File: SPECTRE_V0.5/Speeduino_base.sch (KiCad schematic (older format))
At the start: 209 parts, among them J1 Conn_01x04_Male, J2 Conn_02x04_Odd_Even, J3 Conn_01x06_Male, Q1 2N7002, Q10 BSP78, Q11 BSP78, Q12 BSP78, Q13 BSP78, Q14 BSP78, Q15 BSP78, Q16 SMD-MOSFET-N-CH-55V-2.1A-AO34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, Q17 AO3401A, Q18 BSP78, Q19 SMD-MOSFET-N-CH-55V-2.1A-AO34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, Q2 CJ2302, Q20 AO3401A, Q21 SMD-MOSFET-N-CH-55V-2.1A-AO34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, Q22 SMD-MOSFET-N-CH-55V-2.1A-AO34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, Q23 AO3401A, Q24 AO3401A, Q25 BSP78, Q26 BSP78, Q3 CJ2302, Q4 CJ2302, Q5 BSP78, Q6 BSP78, Q7 CJ2302, Q8 CJ2302, Q9 CJ2302, U1 MAX9926UAEE+, U2 molex_48pin, U3 LM78M05_TO220, U4 MAX3232

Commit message: Somem ore routing V0.5
Routing board V0.5
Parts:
- added JP5: Jumper_NC_Small, Jumper:SolderJumper-2_P1.3mm_Bridged_Pad1.0x1.5mm, symbol Device:Jumper_NC_Small
- added R97: 120, Speeduino_base:R0603, symbol Speeduino_base-eagle-import:SMD-RES-470R-5%-1_10W(0603)
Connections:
- wire segments 549 -> 559
- no-connect marks 54 -> 51
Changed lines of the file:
@@
 Wire Wire Line
 	9900 11100 10350 11100
-Text GLabel 11300 11100 2    50   Input ~ 0
+Text GLabel 10350 11100 2    50   Input ~ 0
 VBAT_F1
 Text GLabel 10450 10700 2    50   Input ~ 0
@@
 NoConn ~ 9600 2800
 NoConn ~ 10500 4000
-NoConn ~ 10200 4800
 NoConn ~ 10200 4900
 NoConn ~ 10200 5000
 NoConn ~ 12050 5000
 NoConn ~ 10500 5000
-NoConn ~ 10500 4500
-NoConn ~ 10200 4500
-NoConn ~ 10500 4400
 NoConn ~ 12050 3300
 NoConn ~ 11750 3400
@@
 $EndComp
 NoConn ~ 11000 6450
-Text GLabel 12050 6250 2    50   Output ~ 0
+Text GLabel 12350 6100 2    50   BiDi ~ 0
 CANL
-Text GLabel 12050 6350 2    50   Output ~ 0
+Text GLabel 12350 6500 2    50   BiDi ~ 0
 CANH
-Text GLabel 6900 1400 3    50   Input ~ 0
+Text GLabel 6900 1400 3    50   BiDi ~ 0
 CANH
-Text GLabel 8700 1400 3    50   Input ~ 0
+Text GLabel 8700 1400 3    50   BiDi ~ 0
 CANL
 Text GLabel 11500 5900 2    50   Input ~ 0
@@
 Wire Wire Line
 	5550 1750 5550 1400
+$Comp
+L Device:Jumper_NC_Small JP5
+U 1 1 5E9CEF08
+P 12450 6400
+F 0 "JP5" H 12450 6612 50  0000 C CNN
+F 1 "Jumper_NC_Small" H 12450 6521 50  0000 C CNN
+F 2 "Jumper:SolderJumper-2_P1.3mm_Bridged_Pad1.0x1.5mm" H 12450 6400 50  0001 C CNN
+F 3 "~" H 12450 6400 50  0001 C CNN
+	1    12450 6400
+	1    0    0    -1
+$EndComp
+$Comp
+L Speeduino_base-eagle-import:SMD-RES-470R-5%-1_10W(0603) R97
+U 1 1 5E9D0C9F
+P 12450 6250
+F 0 "R97" H 12300 6300 42  0000 L BNN
+F 1 "120" H 12300 6150 42  0000 L BNN
+F 2 "Speeduino_base:R0603" H 12450 6250 50  0001 C CNN
+F 3 "" H 12450 6250 50  0001 C CNN
+	1    12450 6250
+	-1   0    0    1
+$EndComp
+Wire Wire Line
+	12600 6250 12650 6250
+Wire Wire Line
+	12650 6250 12650 6400
+Wire Wire Line
+	12650 6400 12550 6400
+Wire Wire Line
+	12350 6100 12300 6100
+Wire Wire Line
+	12300 6100 12300 6250
+Wire Wire Line
+	12350 6400 12350 6500
+Wire Wire Line
+	12050 6350 12250 6350
+Wire Wire Line
+	12250 6350 12250 6400
+Wire Wire Line
+	12250 6400 12350 6400
+Connection ~ 12350 6400
+Wire Wire Line
+	12300 6250 12050 6250
+Connection ~ 12300 6250
+NoConn ~ 10200 4500
 $EndSCHEMATC

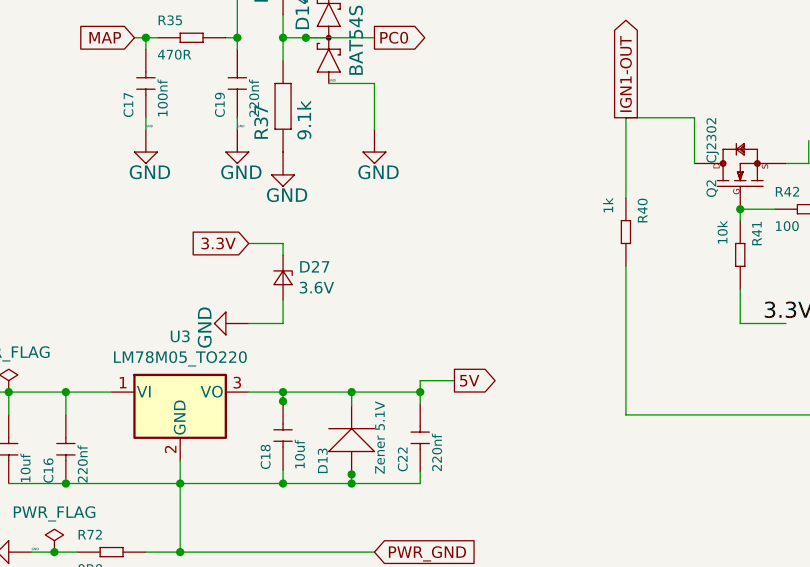
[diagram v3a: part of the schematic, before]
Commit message: 3.3V power protection
Extra protection for the 3.3volt supply. TL431 is used for this.
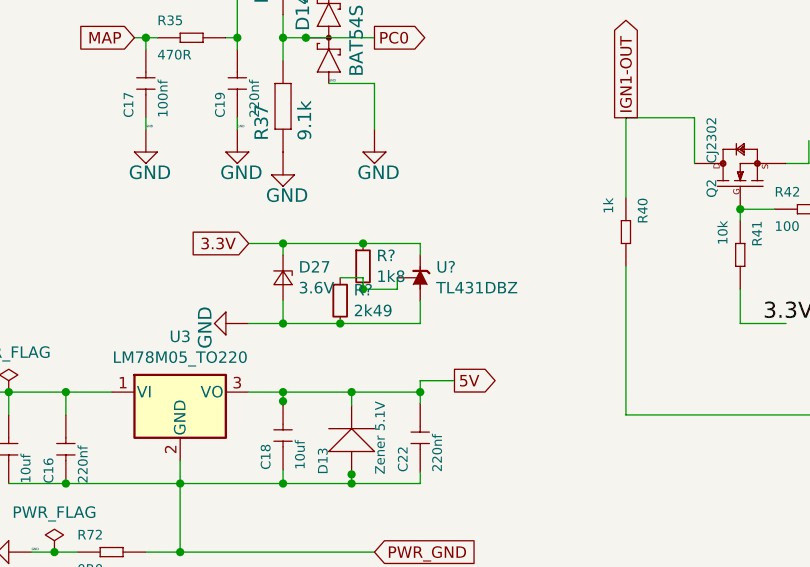
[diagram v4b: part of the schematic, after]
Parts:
- added R?: 1k8, Resistor_SMD:R_0603_1608Metric_Pad1.05x0.95mm_HandSolder, symbol Device:R_Small
- added R?: 2k49, Resistor_SMD:R_0603_1608Metric_Pad1.05x0.95mm_HandSolder, symbol Device:R_Small
- added U?: TL431DBZ, Package_TO_SOT_SMD:SOT-23, symbol Reference_Voltage:TL431DBZ
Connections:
- wire segments 559 -> 569
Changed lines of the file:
@@
 Connection ~ 12300 6250
 NoConn ~ 10200 4500
+$Comp
+L Reference_Voltage:TL431DBZ U?
+U 1 1 5EC38137
+P 3750 10300
+F 0 "U?" V 3796 10230 50  0000 R CNN
+F 1 "TL431DBZ" V 3705 10230 50  0000 R CNN
+F 2 "Package_TO_SOT_SMD:SOT-23" H 3750 10150 50  0001 C CIN
+F 3 "http://www.ti.com/lit/ds/symlink/tl431.pdf" H 3750 10300 50  0001 C CIN
+	1    3750 10300
+	0    -1   -1   0
+$EndComp
+Wire Wire Line
+	3150 10150 3500 10150
+Wire Wire Line
+	3750 10150 3750 10200
+Connection ~ 3150 10150
+Wire Wire Line
+	3750 10400 3750 10500
+Wire Wire Line
+	3750 10500 3400 10500
+Connection ~ 3150 10500
+$Comp
+L Device:R_Small R?
+U 1 1 5ECE80FF
+P 3500 10250
+F 0 "R?" H 3559 10296 50  0000 L CNN
+F 1 "1k8" H 3559 10205 50  0000 L CNN
+F 2 "Resistor_SMD:R_0603_1608Metric_Pad1.05x0.95mm_HandSolder" H 3500 10250 50  0001 C CNN
+F 3 "~" H 3500 10250 50  0001 C CNN
+	1    3500 10250
+	1    0    0    -1
+$EndComp
+Connection ~ 3500 10150
+Wire Wire Line
+	3500 10150 3750 10150
+$Comp
+L Device:R_Small R?
+U 1 1 5ECEB0D8
+P 3400 10400
+F 0 "R?" H 3459 10446 50  0000 L CNN
+F 1 "2k49" H 3459 10355 50  0000 L CNN
+F 2 "Resistor_SMD:R_0603_1608Metric_Pad1.05x0.95mm_HandSolder" H 3400 10400 50  0001 C CNN
+F 3 "~" H 3400 10400 50  0001 C CNN
+	1    3400 10400
+	1    0    0    -1
+$EndComp
+Connection ~ 3400 10500
+Wire Wire Line
+	3400 10500 3150 10500
+Wire Wire Line
+	3400 10300 3500 10300
+Wire Wire Line
+	3500 10300 3500 10350
+Wire Wire Line
+	3500 10350 3650 10350
+Wire Wire Line
+	3650 10350 3650 10300
+Connection ~ 3500 10350
 $EndSCHEMATC

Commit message: Update Speeduino_base.sch
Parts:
- gave numbers to parts that had none: 3
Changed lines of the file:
@@
 NoConn ~ 10200 4500
 $Comp
-L Reference_Voltage:TL431DBZ U?
+L Reference_Voltage:TL431DBZ U5
 U 1 1 5EC38137
 P 3750 10300
-F 0 "U?" V 3796 10230 50  0000 R CNN
+F 0 "U5" V 3796 10230 50  0000 R CNN
 F 1 "TL431DBZ" V 3705 10230 50  0000 R CNN
 F 2 "Package_TO_SOT_SMD:SOT-23" H 3750 10150 50  0001 C CIN
@@
 Connection ~ 3150 10500
 $Comp
-L Device:R_Small R?
+L Device:R_Small R99
 U 1 1 5ECE80FF
 P 3500 10250
-F 0 "R?" H 3559 10296 50  0000 L CNN
+F 0 "R99" H 3559 10296 50  0000 L CNN
 F 1 "1k8" H 3559 10205 50  0000 L CNN
 F 2 "Resistor_SMD:R_0603_1608Metric_Pad1.05x0.95mm_HandSolder" H 3500 10250 50  0001 C CNN
@@
 	3500 10150 3750 10150
 $Comp
-L Device:R_Small R?
+L Device:R_Small R98
 U 1 1 5ECEB0D8
 P 3400 10400
-F 0 "R?" H 3459 10446 50  0000 L CNN
+F 0 "R98" H 3459 10446 50  0000 L CNN
 F 1 "2k49" H 3459 10355 50  0000 L CNN
 F 2 "Resistor_SMD:R_0603_1608Metric_Pad1.05x0.95mm_HandSolder" H 3400 10400 50  0001 C CNN

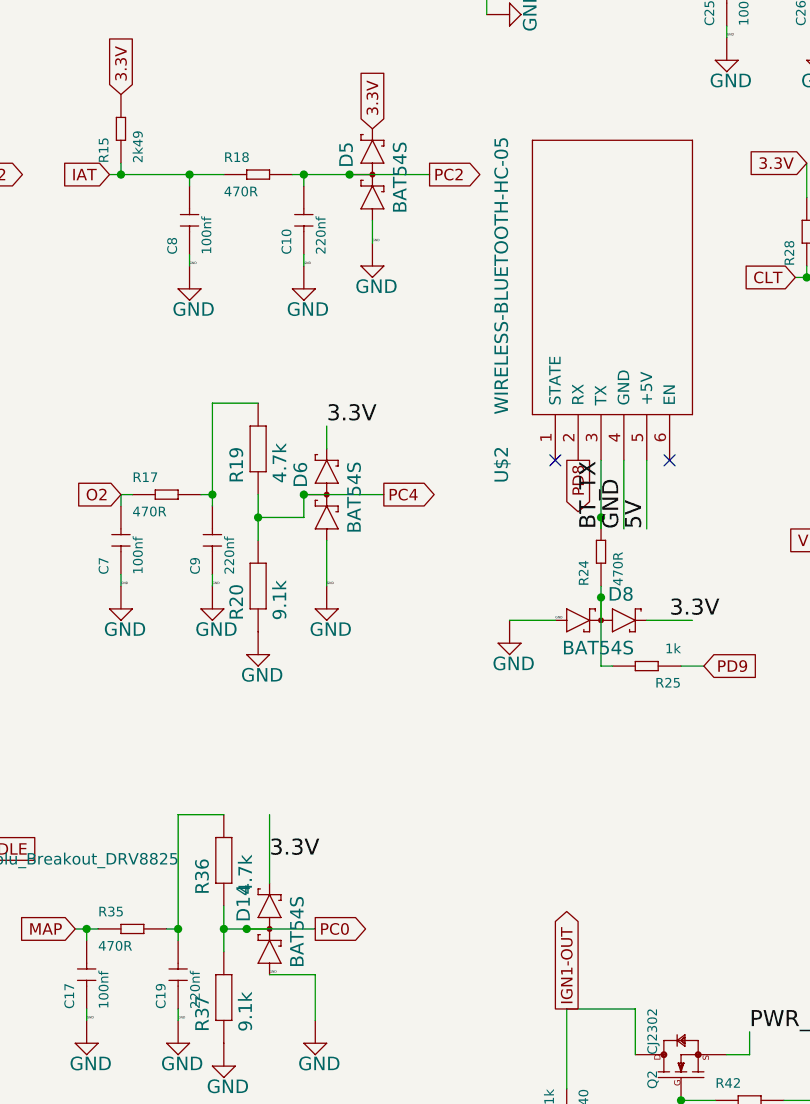
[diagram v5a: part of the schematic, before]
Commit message: V0.5 fully routed
Routed the whole SPECTRE V0.5 board
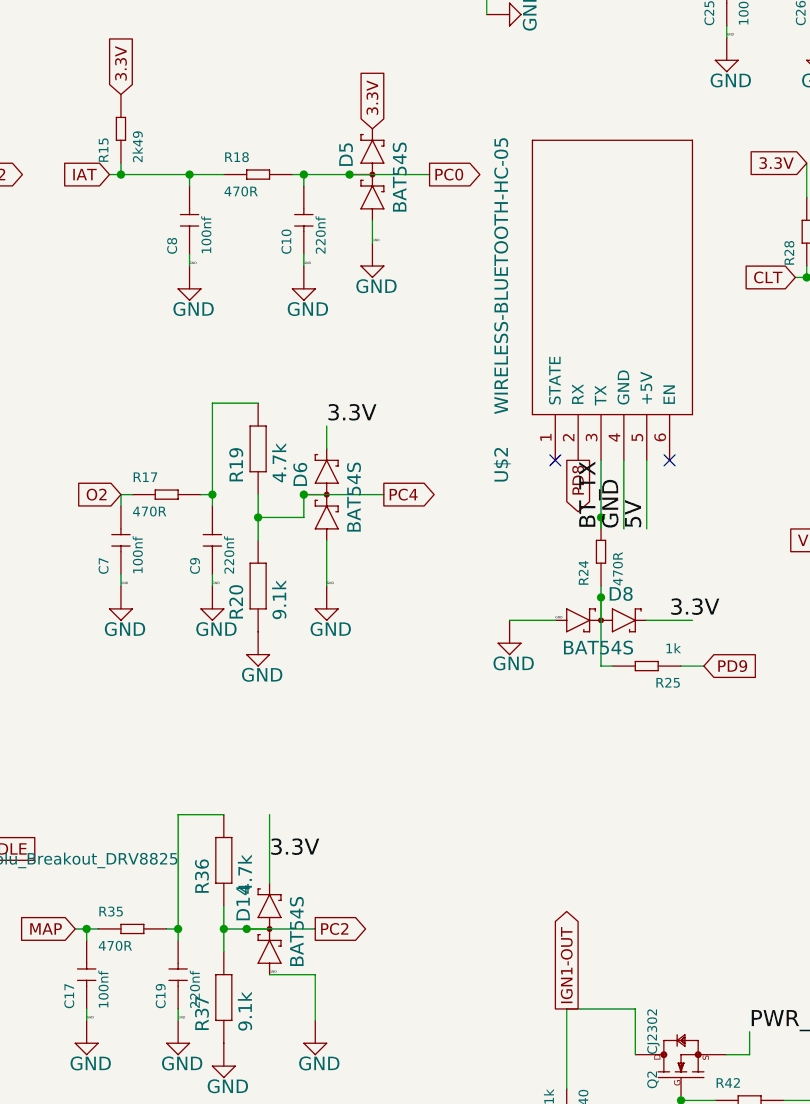
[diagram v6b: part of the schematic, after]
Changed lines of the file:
@@
 Text GLabel 3800 5750 1    50   Input ~ 0
 3.3V
-Text GLabel 4050 5950 2    50   Output ~ 0
+Text GLabel 3550 9250 2    50   Output ~ 0
 PC2
 Wire Wire Line
@@
 Text GLabel 2500 9250 0    50   Input ~ 0
 MAP
-Text GLabel 3550 9250 2    50   Output ~ 0
+Text GLabel 4050 5950 2    50   Output ~ 0
 PC0
 Wire Wire Line

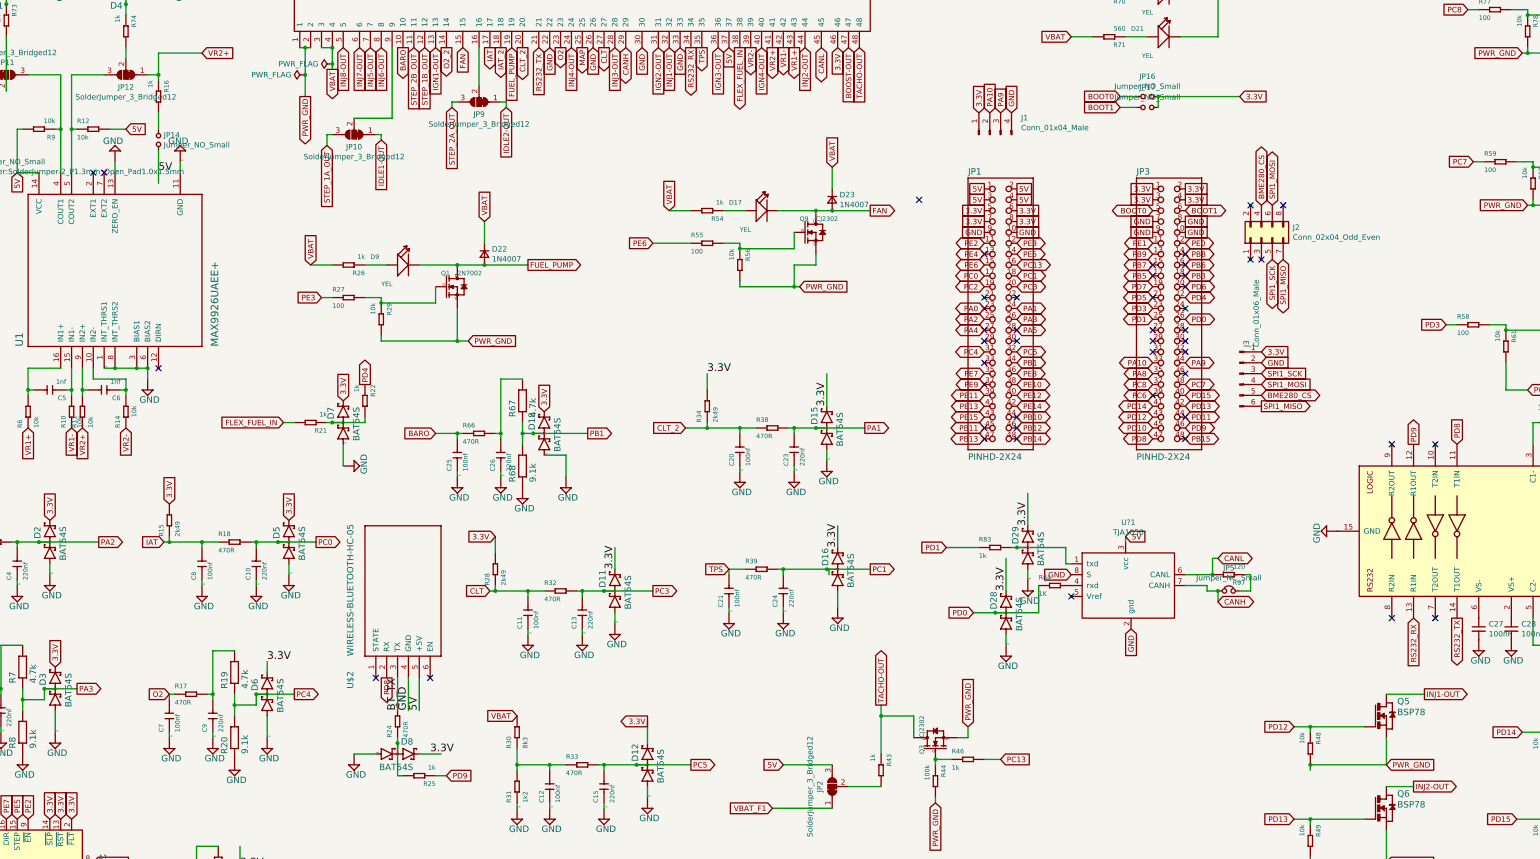
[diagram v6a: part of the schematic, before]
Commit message: updated bluetooth
Now bluetooth is not on second serial anymore. Bluetooth is on Serial1
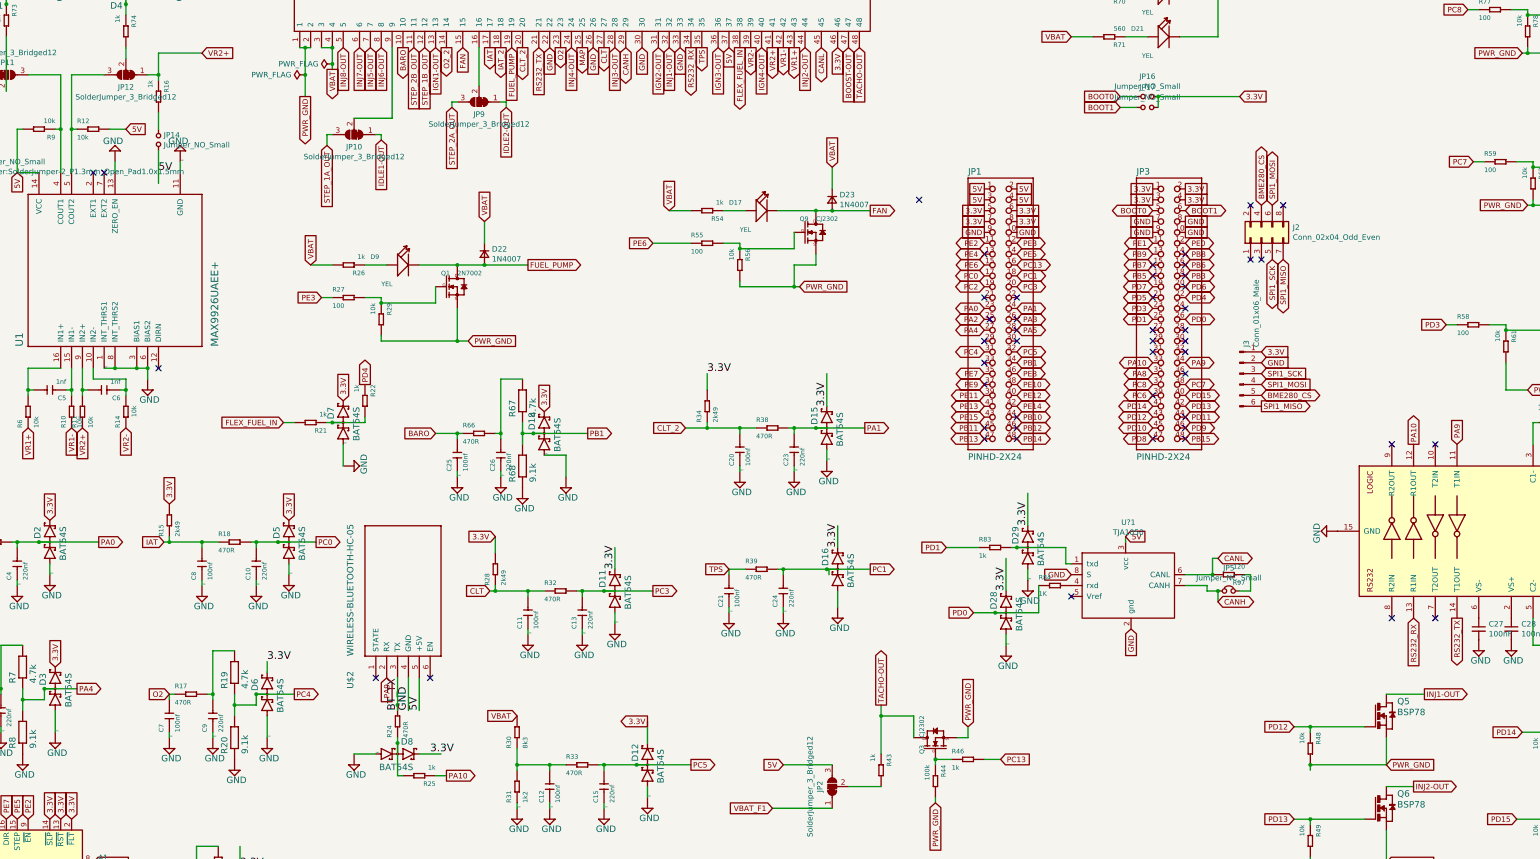
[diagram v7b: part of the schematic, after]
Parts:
- removed J1: Conn_01x04_Male, Connector_PinHeader_2.00mm:PinHeader_1x04_P2.00mm_Vertical_SMD_Pin1Left, symbol Connector:Conn_01x04_Male
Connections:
- no-connect marks 51 -> 53
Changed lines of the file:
@@
 PB1
 Text GLabel 1850 7300 2    50   Output ~ 0
-PA3
+PA4
 Text GLabel 13050 7650 0    50   Input ~ 0
 PD12
@@
 	15350 8500 15850 8500
 Text GLabel 2050 5950 2    50   Output ~ 0
-PA2
+PA0
 Text GLabel 9100 4900 2    50   Output ~ 0
 PA1
@@
 Wire Wire Line
 	2050 11500 2150 11500
-$Comp
-L Connector:Conn_01x04_Male J1
-U 1 1 5E2F31E3
-P 10250 2200
-F 0 "J1" V 10404 1912 50  0000 R CNN
-F 1 "Conn_01x04_Male" V 10313 1912 50  0000 R CNN
-F 2 "Connector_PinHeader_2.00mm:PinHeader_1x04_P2.00mm_Vertical_SMD_Pin1Left" H 10250 2200 50  0001 C CNN
-F 3 "~" H 10250 2200 50  0001 C CNN
-	1    10250 2200
-	0    -1   -1   0
-$EndComp
-Text GLabel 10150 2000 1    50   Input ~ 0
-3.3V
-Text GLabel 10450 2000 1    50   Input ~ 0
-GND
-Text GLabel 10250 2000 1    50   Input ~ 0
-PA10
-Text GLabel 10350 2000 1    50   Input ~ 0
-PA9
 $Comp
 L Device:D_Small D24
@@
 	2550 9250 2600 9250
 NoConn ~ 10200 3700
-NoConn ~ 10200 3800
 NoConn ~ 10200 4300
 Text GLabel 4100 3700 0    50   Input ~ 0
@@
 NoConn ~ 11750 4100
 NoConn ~ 11750 4200
-Text GLabel 5250 8100 2    50   Input ~ 0
-PD9
-Text GLabel 4700 7200 3    50   Output ~ 0
-PD8
+Text GLabel 5250 8100 2    50   Output ~ 0
+PA10
 NoConn ~ 4600 7200
 NoConn ~ 5100 7200
@@
 	1    0    0    -1
 $EndComp
-NoConn ~ 10200 4000
 NoConn ~ 9600 2800
 NoConn ~ 10500 4000
@@
 	1    0    0    -1
 $EndComp
-Text GLabel 14150 5050 1    50   Output ~ 0
-PD9
 Text GLabel 14150 6650 3    50   Input ~ 0
 RS232_RX
@@
 Text GLabel 14550 6650 3    50   Output ~ 0
 RS232_TX
-Text GLabel 14550 5050 1    50   Input ~ 0
-PD8
 $Comp
 L speeduino_lib:SMD-MOSFET-N-CH-30V-5.8A-AO3400(SOT-23) Q19
@@
 	3650 10350 3650 10300
 Connection ~ 3500 10350
+Text GLabel 14550 5050 1    50   Input ~ 0
+PA9
+Text GLabel 14150 5050 1    50   Output ~ 0
+PA10
+Text GLabel 4700 7200 3    50   Input ~ 0
+PA9
+NoConn ~ 11750 5000
+NoConn ~ 12050 4900
+NoConn ~ 10250 3900
+NoConn ~ 10500 3900
 $EndSCHEMATC
